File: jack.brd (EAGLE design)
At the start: 100 x 80 mm, 30 parts, among them IC1 NUF2221W1T2G, IC2 ATSAMD21G18, IC3 LDO, SW1 SPST3.5X6MM, X1 TSX-3225 24.0000MF10Z-C3

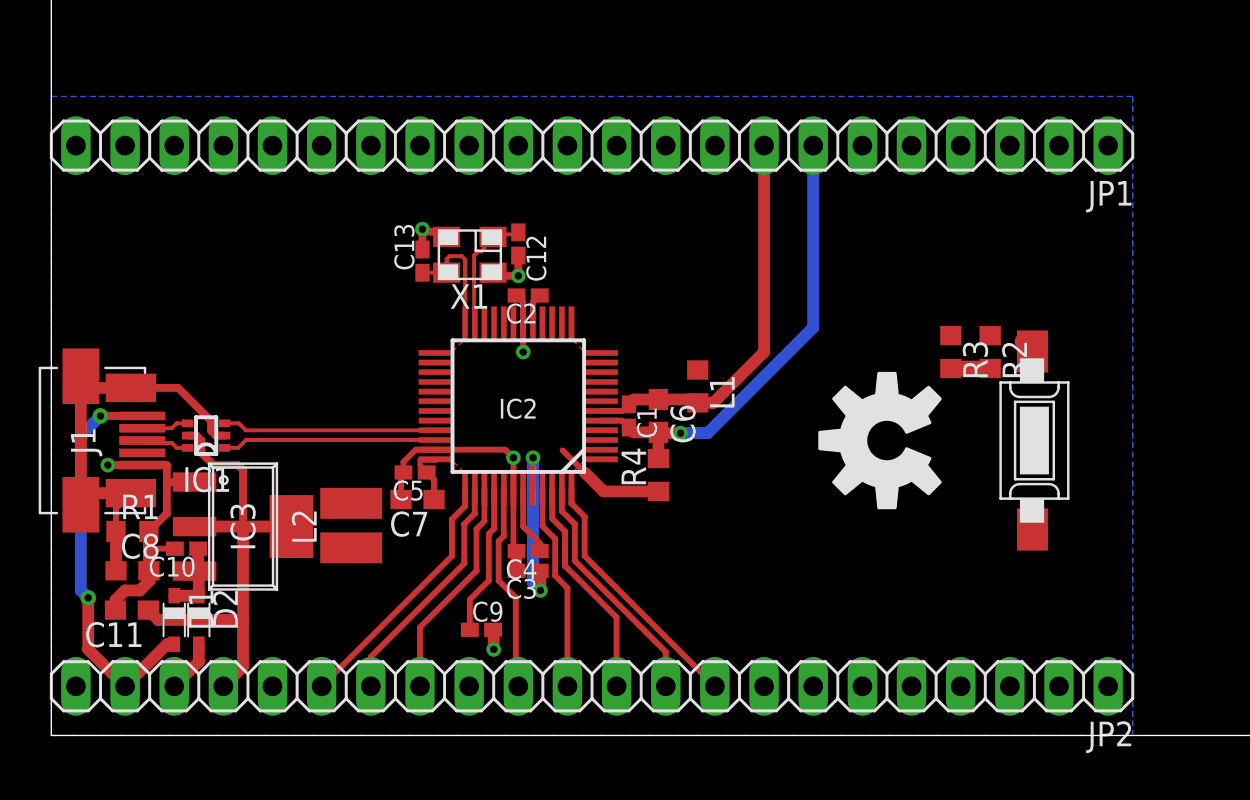
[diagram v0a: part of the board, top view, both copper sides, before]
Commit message: PCB layout almost done, changed breakout configuration accordingly
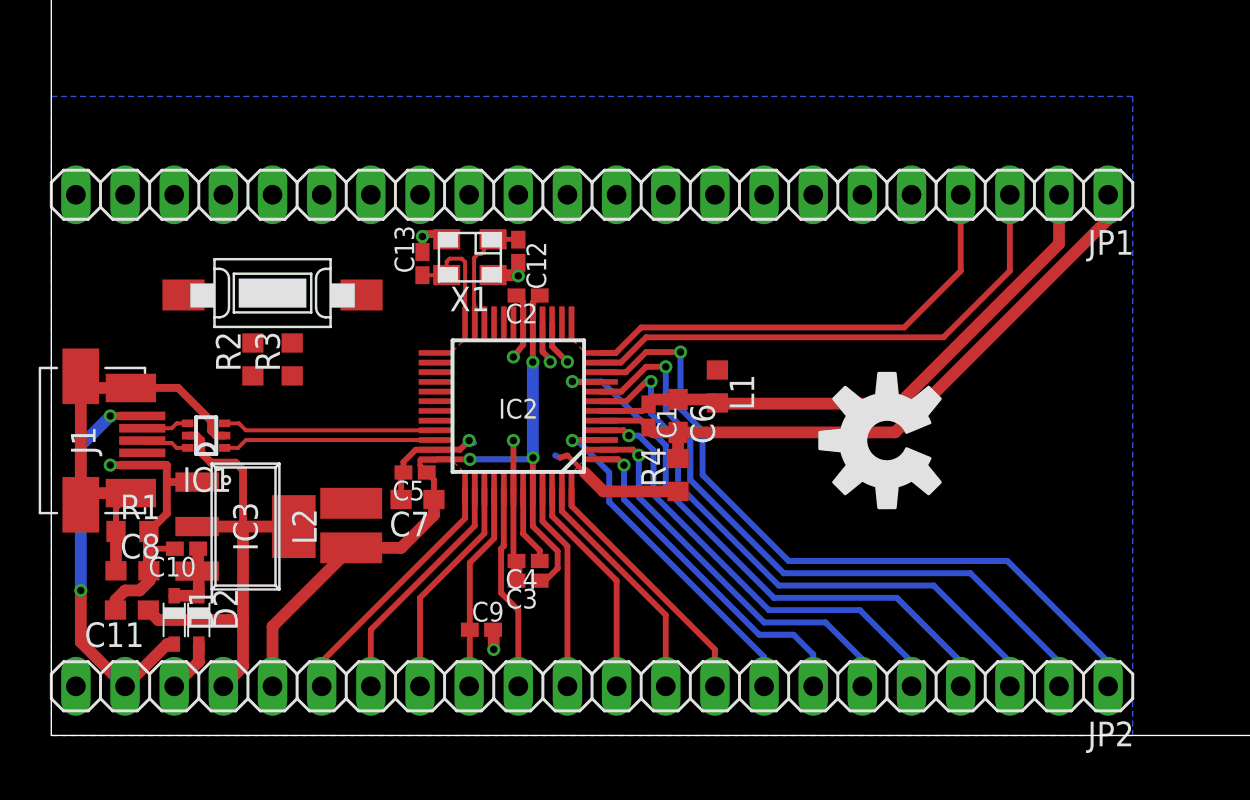
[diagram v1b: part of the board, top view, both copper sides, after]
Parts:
- moved SW1 40.1 mm to (11.4, 22.9), turned to 180 degrees
- moved R2 38.1 mm to (10.4, 19.4), turned to 90 degrees
- moved R3 34.0 mm to (12.4, 19.4), turned to 90 degrees
- moved JP1 2.54 mm to (27.9, 27.9)
- moved C1 1.02 mm to (30.9, 16.5)
- moved C6 1.02 mm to (32.4, 16.5)
- moved L1 1.02 mm to (34.4, 18.0)
- moved R4 1.02 mm to (32.4, 13.5)
- moved C3 0.51 mm to (24.6, 8.00)
- moved C4 0.51 mm to (24.6, 9.02)
- moved C12 0.38 mm to (24.1, 25.0)
- moved C13 0.13 mm to (19.2, 24.4)
- moved IC3 0.13 mm to (10.0, 10.8)
- moved X1 0.13 mm to (21.6, 24.7)
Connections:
- new net NC: JP1.10, JP1.11, JP1.12, JP1.13, JP1.14, JP1.15, JP1.16, JP1.17, JP1.18, JP1.9
- net 1: now also JP2.7; no longer JP1.3
- net 10: now also JP2.1; no longer JP1.12
- net 11: now also JP1.3; no longer JP1.13
- net 12: now also JP1.4; no longer JP1.14
- net 13: now also JP1.5; no longer JP1.15
- net 14: now also JP1.6; no longer JP1.16
- net 15: now also JP1.7; no longer JP1.17
- net 16: now also JP1.8; no longer JP1.18
- net 2: now also JP2.6; no longer JP1.4
- net 25: no longer JP2.1
- net 26: no longer JP2.2
- net 27: no longer JP2.3
- net 28: no longer JP2.4
- net 29: no longer JP2.5
- net 3: now also JP2.8; no longer JP1.5
- net 30: no longer JP2.6
- net 31: no longer JP2.7
- net 32: no longer JP2.8
- net 4: now also JP2.5; no longer JP1.6
- net 7: now also JP2.3; no longer JP1.9
- net 8: now also JP2.2; no longer JP1.10
- net 9: now also JP2.4; no longer JP1.11
- net GND: no longer JP1.1
- net GNDANA: now also JP1.1; no longer JP1.7
- net VDDANA: now also JP1.2; no longer JP1.8
- net VDDF: no longer JP1.2
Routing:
- net 10: track 0.00 -> 37.6 mm, vias 0 -> 1
- net 8: track 0.00 -> 34.7 mm, vias 0 -> 1
- net 7: track 0.00 -> 31.1 mm, vias 0 -> 1
- net 9: track 0.00 -> 30.3 mm, vias 0 -> 1
- net 11: track 0.00 -> 27.0 mm
- net VDDF: track 14.4 -> 38.9 mm, vias 2 -> 3
- net 12: track 0.00 -> 24.3 mm
- net 4: track 0.00 -> 23.6 mm, vias 0 -> 1
- net 2: track 0.00 -> 21.2 mm, vias 0 -> 1
- net 3: track 0.00 -> 18.4 mm, vias 0 -> 1
- net 1: track 0.00 -> 18.0 mm, vias 0 -> 1
- net VDDANA: track 20.5 -> 30.0 mm
- net GNDANA: track 24.3 -> 33.7 mm, vias 1 -> 0
- net 15: track 0.00 -> 2.29 mm, vias 0 -> 1
- net 16: track 0.00 -> 2.26 mm, vias 0 -> 1
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
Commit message: :feelsgood: Layout finished!
Minor details gotta be worked now (polishing pours layout)
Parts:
- JP1, JP2: value (none) -> PINHD-1X21; device pinhead:1X22 -> jack:1X21
- moved JP1 25.4 mm to (26.7, 2.54)
- moved JP2 25.4 mm to (26.7, 27.9), turned to 0 degrees
- moved R2 3.18 mm to (7.37, 20.3), turned to 270 degrees
- moved R3 2.57 mm to (9.91, 19.8), turned to 180 degrees
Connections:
- removed net NC: JP1.10, JP1.11, JP1.12, JP1.13, JP1.14, JP1.15, JP1.16, JP1.17, JP1.18, JP1.9
- net !RESET: now also JP1.13; no longer JP2.14
- net 1: now also JP1.6; no longer JP2.7
- net 10: now also JP2.19; no longer JP2.1
- net 11: now also JP2.18; no longer JP1.3
- net 12: now also JP2.17; no longer JP1.4
- net 13: now also JP2.16; no longer JP1.5
- net 14: now also JP2.15; no longer JP1.6
- net 15: now also JP2.14; no longer JP1.7
- net 16: now also JP2.13; no longer JP1.8
- net 19: now also JP2.12; no longer JP1.19
- net 2: now also JP1.5; no longer JP2.6
- net 20: now also JP2.11; no longer JP1.20
- net 21: now also JP2.10; no longer JP1.21
- net 22: now also JP2.9; no longer JP1.22
- net 25: now also JP2.8
- net 26: now also JP2.7
- net 27: now also JP2.6
- net 28: now also JP2.5
- net 29: now also JP2.4
- net 3: now also JP1.7; no longer JP2.8
- net 30: now also JP2.3
- net 31: now also JP2.2
- net 32: now also JP2.1
- net 37: now also JP1.16; no longer JP2.17
- net 38: now also JP1.15; no longer JP2.16
- net 39: now also JP1.14; no longer JP2.15
- net 4: now also JP1.4; no longer JP2.5
- net 41: now also JP1.12; no longer JP2.13
- net 47: now also JP1.9; no longer JP2.10
- net 48: now also JP1.8; no longer JP2.9
- net 7: now also JP1.2; no longer JP2.3
- net 8: now also JP1.1; no longer JP2.2
- net 9: now also JP1.3; no longer JP2.4
- net GND: now also JP1.21; no longer JP2.22
- net GNDANA: now also JP2.21; no longer JP1.1
- net SWCLK: now also JP1.11; no longer JP2.12
- net SWDIO: now also JP1.10; no longer JP2.11
- net VBUS: now also JP1.20; no longer JP2.21
- net VDD: now also JP1.18; no longer JP2.19
- net VDDANA: now also JP2.20; no longer JP1.2
- net VDDF: now also JP1.17; no longer JP2.18
- net VIN: now also JP1.19; no longer JP2.20
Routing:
- net VDD: track 25.7 -> 59.3 mm, vias 0 -> 4
- net 32: track 0.00 -> 25.0 mm
- net 31: track 0.00 -> 22.2 mm
- net !RESET: track 10.8 -> 31.0 mm, vias 0 -> 2
- net 30: track 0.00 -> 19.7 mm
- net 13: track 0.00 -> 18.1 mm
- net 29: track 0.00 -> 16.5 mm
- net 14: track 0.00 -> 16.2 mm
- net 28: track 0.00 -> 14.8 mm
- net 19: track 0.00 -> 14.2 mm, vias 0 -> 1
- net VDDF: track 38.9 -> 52.9 mm, vias 3 -> 4
- net 15: track 2.29 -> 16.1 mm
- net 20: track 0.00 -> 13.6 mm, vias 0 -> 1
- net 27: track 0.00 -> 13.0 mm
- net 10: track 37.6 -> 24.7 mm, vias 1 -> 0
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- added copper zone on layer 16, net GNDANA
- added copper zone on layer 1, net VDDF
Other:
- board size 100 x 80 mm -> 53.3 x 29.7 mm

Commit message: :thumbsup: minor project update (polishing stuff)
Added new screenshots, little tweaks to schematic and layout (ground
fills, power signals fills). The design is still missing a logo though
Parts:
- J1: value (none) -> USB-micro
- X1: value TSX-3225 24.0000MF10Z-C3 -> CX-3225 12.288MHz
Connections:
- net GND: now also JP1.20; no longer JP1.21
- net VBUS: now also JP1.21; no longer JP1.20
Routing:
- net GND: track 48.4 -> 45.0 mm, vias 6 -> 10
- net VBUS: track 20.8 -> 22.8 mm
- added copper zone on layer 1, net LDOIN

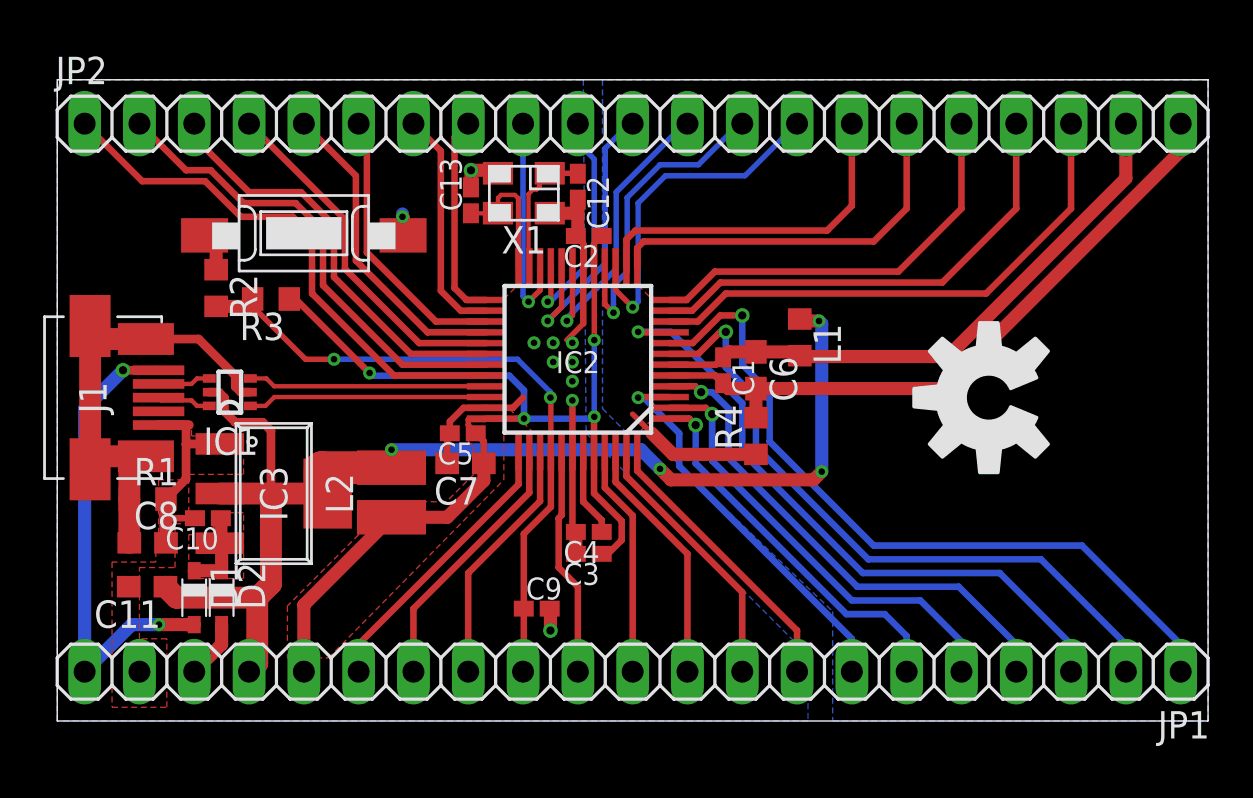
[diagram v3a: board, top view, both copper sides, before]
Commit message: :feelsgood: Totally done now!
Added LED on pin 23, added logos (hackaday, oshw, JACK)
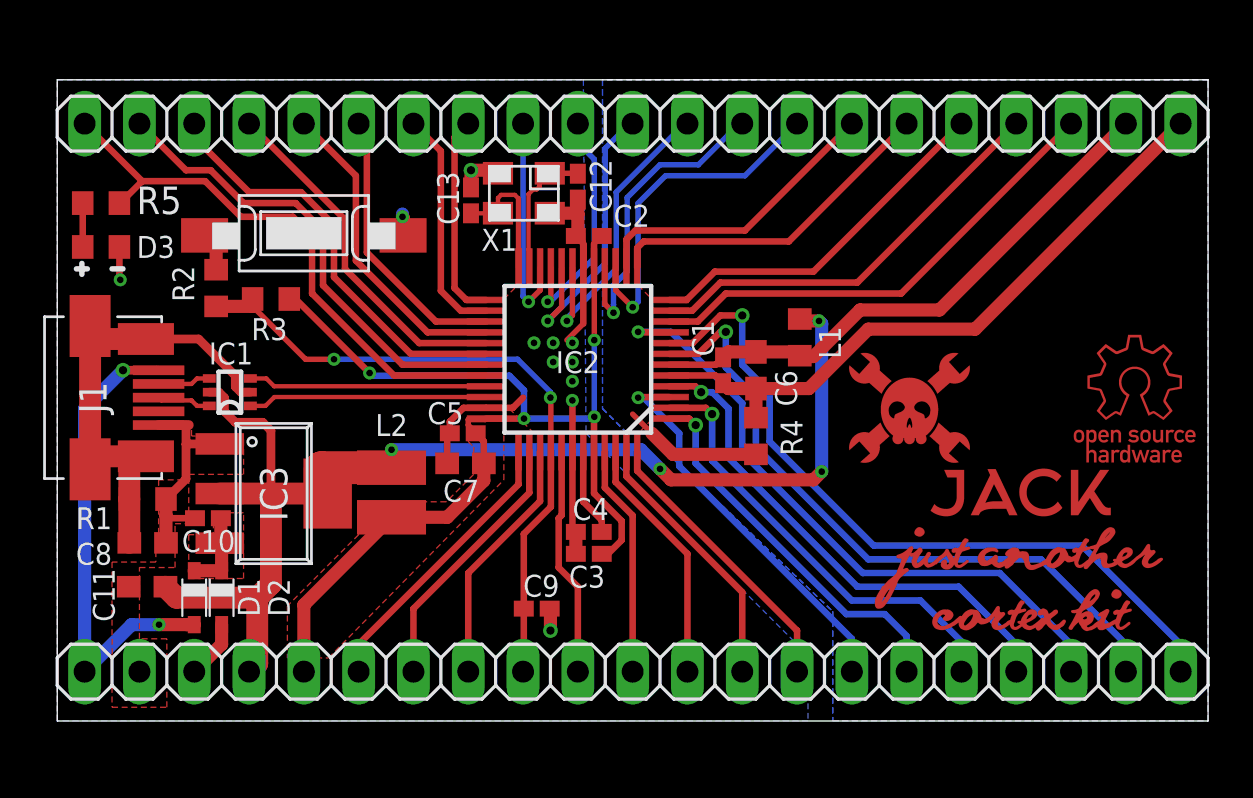
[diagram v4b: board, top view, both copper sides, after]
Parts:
- removed LOGO1: OSHW-LOGOL, SparkFun-Aesthetics:OSHW-LOGO-L
- added D3: LED, jack:LED-0603
- added R5: 90, rcl:R0603
- added U$3: JACK-LOGO, jack:JACK-LOGO
- added U$5: HAD-LOGO, jack:HAD-LOGO
- added U$6: OSHW-LOGO, jack:OSHW-LOGO
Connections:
- new net N$1: D3.A, R5.1
- net 32: now also R5.2
- net GND: now also D3.C
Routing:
- net 13: track 18.1 -> 15.8 mm
- net 12: track 19.2 -> 16.9 mm
- net 11: track 22.0 -> 19.7 mm
- net 10: track 24.7 -> 22.4 mm
- net 14: track 16.2 -> 14.0 mm
- net N$1: track 0.00 -> 2.03 mm
- net GND: track 45.0 -> 46.6 mm, vias 10 -> 11
- net VDDANA: track 27.4 -> 26.0 mm
- net 32: track 25.0 -> 26.5 mm
- net GNDANA: track 31.1 -> 30.4 mm

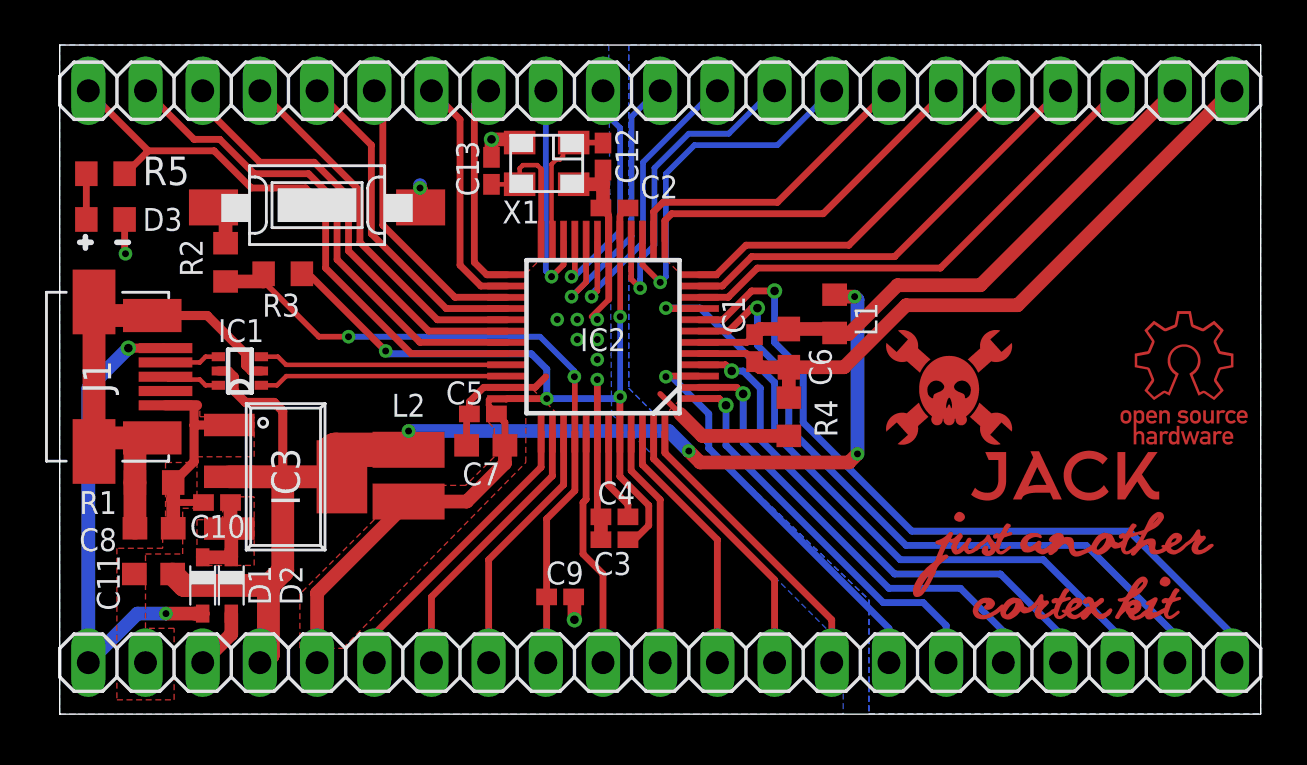
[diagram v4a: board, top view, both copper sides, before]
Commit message: :octocat: Added stopmask on logos
Now the logos will look all shiny and clear! woohoo
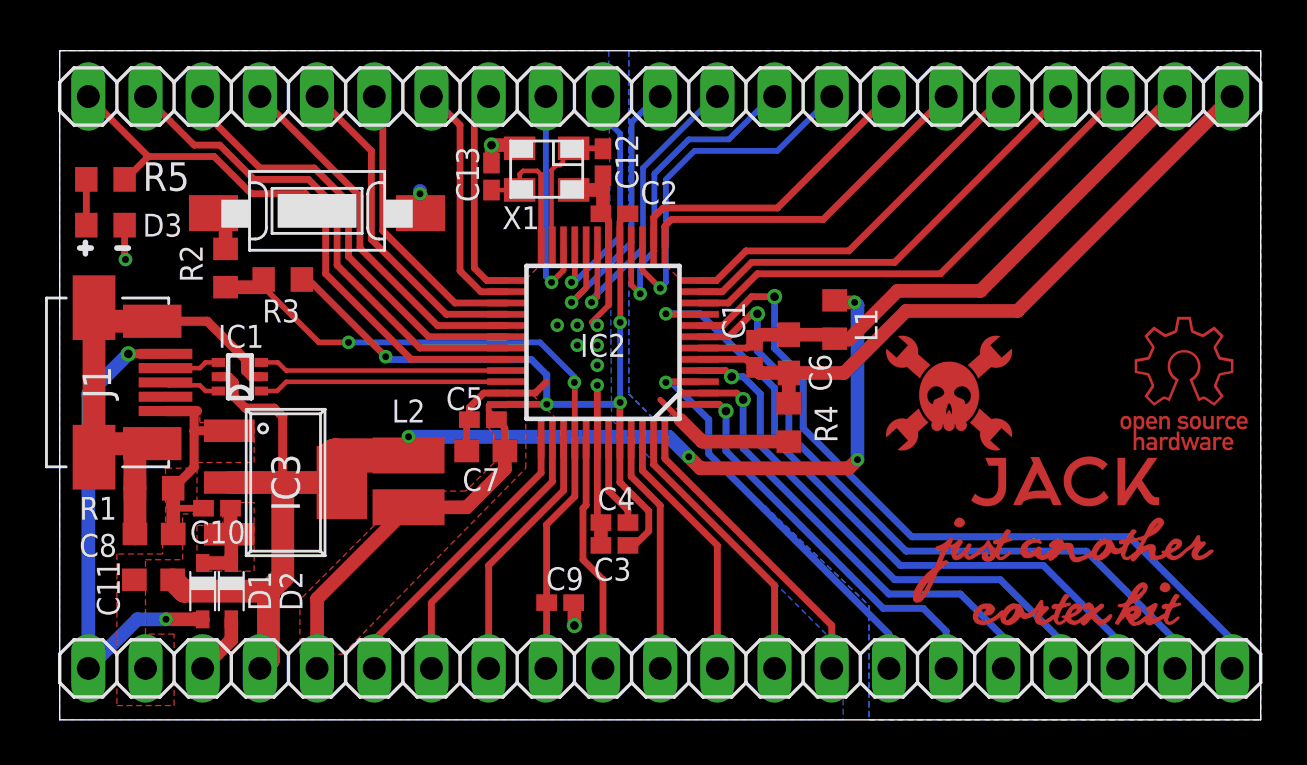
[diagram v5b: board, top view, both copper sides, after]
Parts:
- moved C1 0.25 mm to (30.9, 16.3)
- moved C13 0.25 mm to (19.2, 24.1)
- moved C2 0.25 mm to (24.6, 22.5)
- moved C6 0.25 mm to (32.4, 16.3)
- moved D3 0.25 mm to (2.03, 22.0)
- moved IC2 0.25 mm to (24.1, 16.8)
- moved JP2 0.25 mm to (26.7, 27.7)
- moved R2 0.25 mm to (7.37, 20.1)
- moved R3 0.25 mm to (9.91, 19.6)
- moved R5 0.25 mm to (2.03, 24.0)
- moved U$5 0.25 mm to (39.5, 14.1)
- moved U$6 0.25 mm to (49.9, 15.1)
- moved X1 0.25 mm to (21.6, 24.5)
- moved C11 0.25 mm to (4.17, 6.22)
- moved C9 0.25 mm to (22.2, 5.21)
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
